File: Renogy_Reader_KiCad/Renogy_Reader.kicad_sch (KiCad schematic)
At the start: 25 parts, among them J2 Conn_02x06_Odd_Even, J3 RJ45, Q1 2N7000, Q2 2N7000, Q3 2N7000, U1 ESP32-DEVKIT-V1, U4 DS18B20

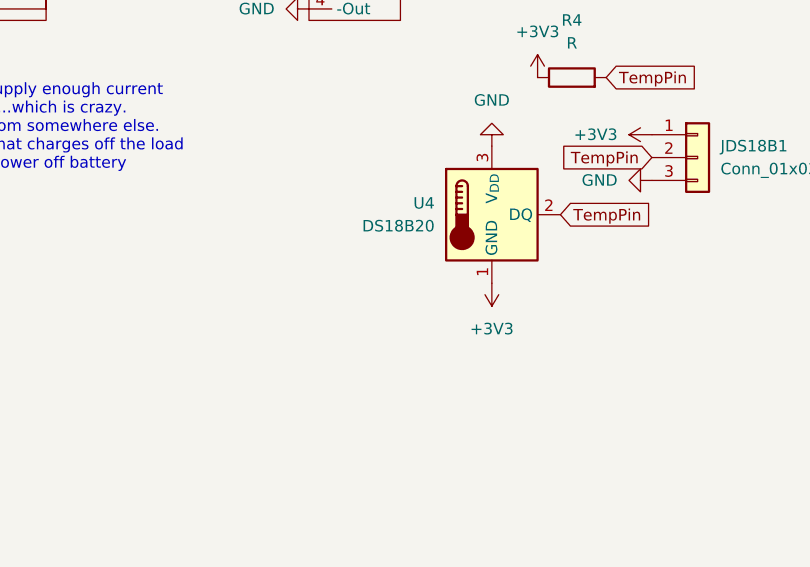
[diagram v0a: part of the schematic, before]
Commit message: added ds18b20 reading
and fixed controller and battery temp reading
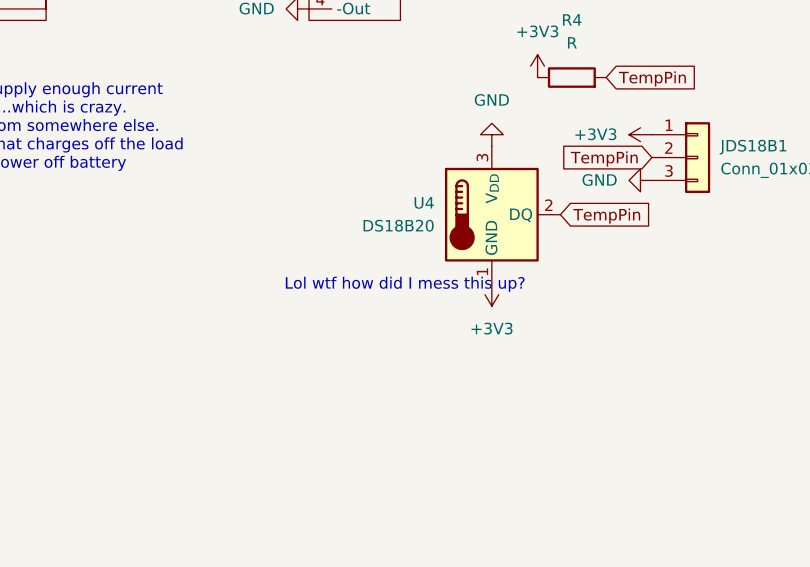
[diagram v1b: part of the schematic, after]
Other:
- note added: "Lol wtf how did I mess this up?"
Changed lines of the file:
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@@
+		)
+	)
+	(text "Lol wtf how did I mess this up?"
+		(exclude_from_sim no)
+		(at 215.138 108.204 0)
+		(effects
+			(font
+				(size 1.27 1.27)
+			)
 		)
 	)

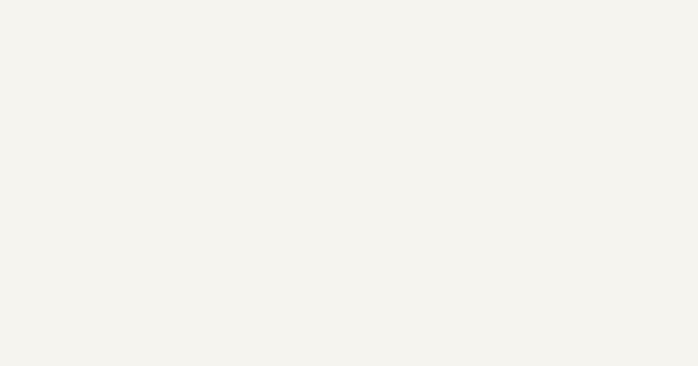
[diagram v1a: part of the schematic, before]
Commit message: updated kicad
Updated kicad to show errors in DS18B20 pins
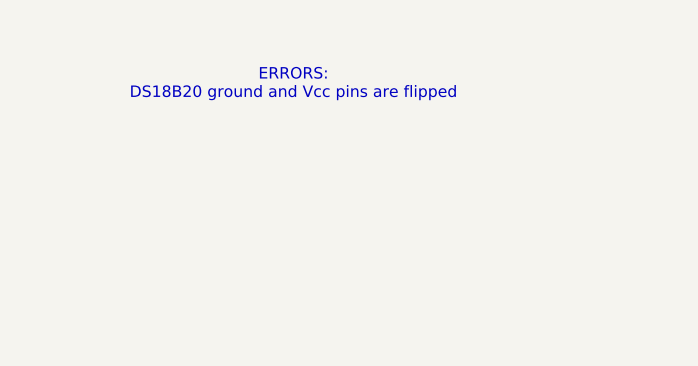
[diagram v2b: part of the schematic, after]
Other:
- note added: "ERRORS: DS18B20 ground and Vcc pins are flipped"
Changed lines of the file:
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@@
+		)
+	)
+	(text "ERRORS:\nDS18B20 ground and Vcc pins are flipped"
+		(exclude_from_sim no)
+		(at 40.132 21.336 0)
+		(effects
+			(font
+				(size 1.27 1.27)
+			)
 		)
 	)
